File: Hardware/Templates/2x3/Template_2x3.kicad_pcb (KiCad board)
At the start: 2 copper layers, 84 x 126 mm, 4 parts

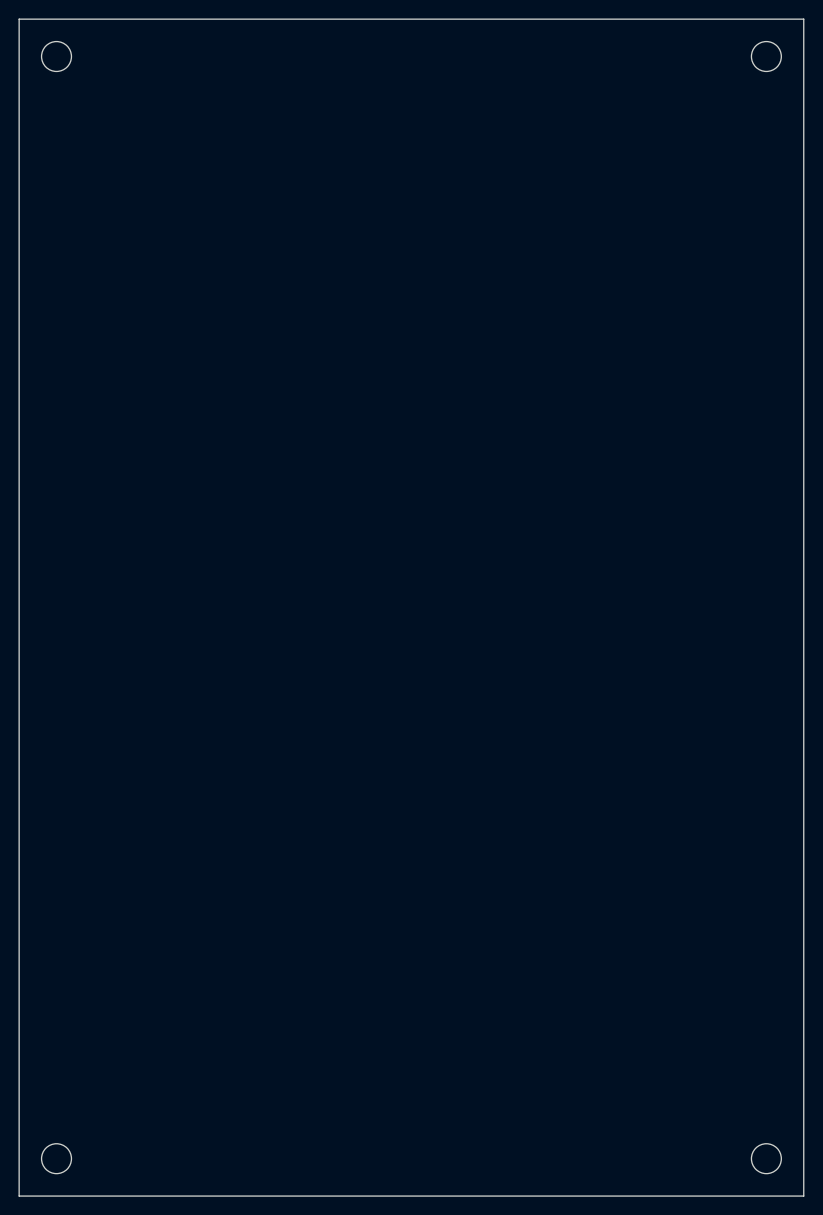
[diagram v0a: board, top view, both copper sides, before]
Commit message: Edited Templates for Hardware
Edited size of templates to fit within containers
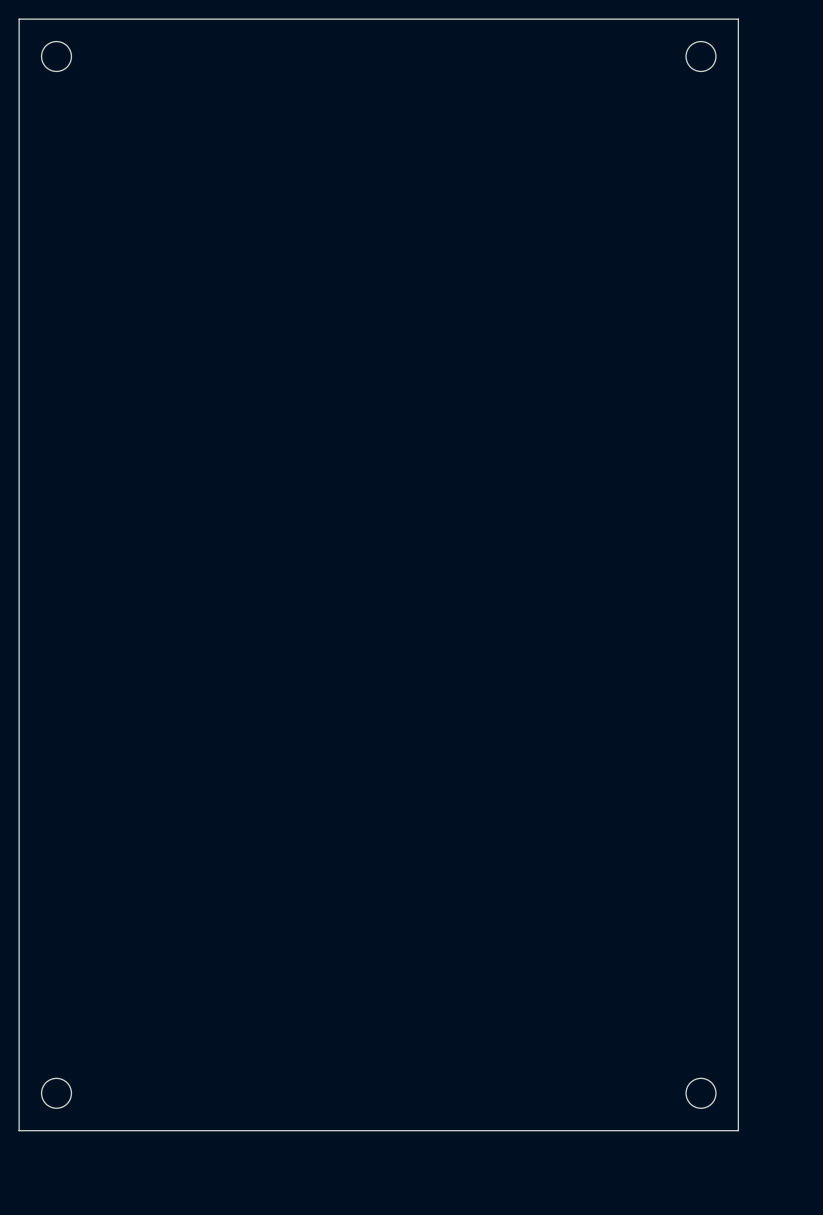
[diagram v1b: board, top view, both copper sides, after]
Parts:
- moved REF** 9.90 mm to (93.0, 135.0)
- moved REF** 7.00 mm to (93.0, 24.0)
- moved REF** 7.00 mm to (24.0, 135.0)
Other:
- board size 84 x 126 mm -> 77 x 119 mm
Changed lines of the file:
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@@
 	(footprint "MountingHole:MountingHole_3.2mm_M3"
 		(layer "F.Cu")
-		(at 100 142)
+		(at 93 135)
 		(descr "Mounting Hole 3.2mm, no annular, M3")
 		(tags "mounting hole 3.2mm no annular m3")
@@
 	(footprint "MountingHole:MountingHole_3.2mm_M3"
 		(layer "F.Cu")
-		(at 100 24)
+		(at 93 24)
 		(descr "Mounting Hole 3.2mm, no annular, M3")
 		(tags "mounting hole 3.2mm no annular m3")
@@
 	(footprint "MountingHole:MountingHole_3.2mm_M3"
 		(layer "F.Cu")
-		(at 24 142)
+		(at 24 135)
 		(descr "Mounting Hole 3.2mm, no annular, M3")
 		(tags "mounting hole 3.2mm no annular m3")
@@
 	(gr_rect
 		(start 20 20)
-		(end 104 146)
+		(end 97 139)
 		(stroke
 			(width 0.1)
